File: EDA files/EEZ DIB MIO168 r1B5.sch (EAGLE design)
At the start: 302 parts, among them IC1 M24C32-WMN6P, IC10 DAC7760IPWPR, IC11 DAC7760IPWPR, IC12 OPA376AIDBVR, IC13 DAC7563TDGSR, IC14 OPA2196IDR, IC15 BTS3408G, IC16 BTS3408G, IC17 BTS3408G, IC18 BTS3408G, IC19 74HC126PW,118, IC2 Si8641BB-B-IS1, IC20 TL431B, IC21 DG468DV-T1-E3, IC22 DG468DV-T1-E3, IC23 DG468DV-T1-E3, IC24 DG468DV-T1-E3, IC25 DG468DV-T1-E3, IC26 DG468DV-T1-E3, IC27 DG468DV-T1-E3, IC28 DG468DV-T1-E3, IC29 DG468DV-T1-E3, IC3 Si8641BB-B-IS1, IC30 DG468DV-T1-E3, IC31 DG468DV-T1-E3, IC32 DG468DV-T1-E3, IC33 DG468DV-T1-E3, IC34 DG468DV-T1-E3, IC35 OPA376AIDBVR, IC36 ADS8674IDBT, IC4 L78L12, IC5 LM1117MP-5.0, IC6 LP2985-33DBVR, IC7 L79L12, IC8 STM32F446ZCT6, IC9 OPA2196IDR, J1 4907, J2 N.C., Q1 2N7002PS,115, Q10 BSS169, Q11 BSS169, Q12 BSS169, Q13 BSS169, Q2 2N7002PS,115, Q3 2N7002PS,115, Q4 2N7002PS,115, Q5 2N7002PS,115, Q6 BSS169, Q7 BSS169, Q8 BSS169, Q9 BSS169, X1 77317-104-28LF, X2 SSW-106-02-S-S, X3 691327310016, X4 691327310016, X5 1-2314878-0, X6 1-2314878-0, X7 1-2314878-0, Y1 25MHz

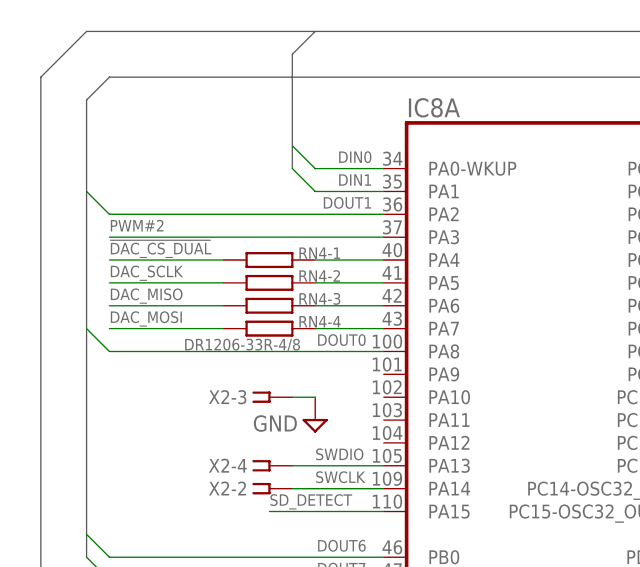
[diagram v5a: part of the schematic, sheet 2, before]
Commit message: swap DOUT0 and DOUT1
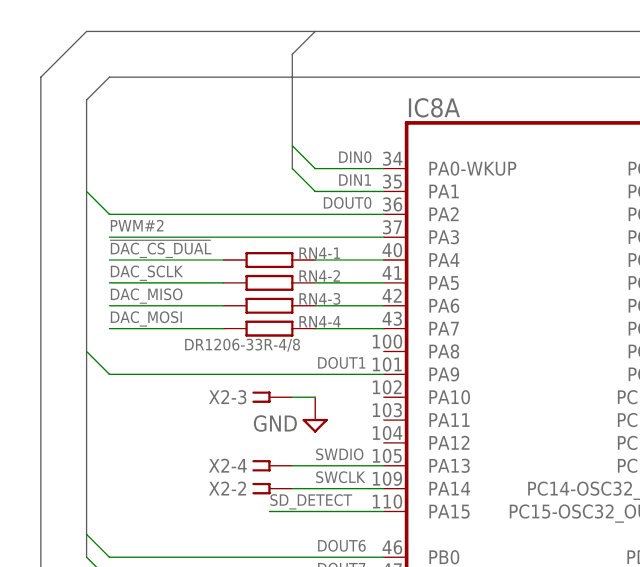
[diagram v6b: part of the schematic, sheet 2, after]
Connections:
- net DOUT0: now also IC8A.PA2; no longer IC8A.PA8
- net DOUT1: now also IC8A.PA9; no longer IC8A.PA2
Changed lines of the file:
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@@
 <setting verticaltext="up"/>
 </settings>
-<grid distance="0.025" unitdist="inch" unit="inch" style="lines" multiple="4" display="no" altdistance="0.01" altunitdist="inch" altunit="inch"/>
+<grid distance="0.1" unitdist="inch" unit="inch" style="lines" multiple="1" display="no" altdistance="0.01" altunitdist="inch" altunit="inch"/>
 <layers>
 <layer number="1" name="Top" color="4" fill="1" visible="no" active="no"/>
@@
 <net name="DOUT0" class="0">
 <segment>
-<wire x1="10.16" y1="142.24" x2="12.7" y2="139.7" width="0.1524" layer="91"/>
-<pinref part="IC8" gate="A" pin="PA8"/>
-<label x="41.275" y="140.335" size="1.27" layer="102" rot="MR0"/>
-<wire x1="12.7" y1="139.7" x2="43.18" y2="139.7" width="0.1524" layer="91"/>
-</segment>
-</net>
-<net name="DOUT1" class="0">
-<segment>
 <pinref part="IC8" gate="A" pin="PA2"/>
 <wire x1="43.18" y1="154.94" x2="12.7" y2="154.94" width="0.1524" layer="91"/>
@@
 </segment>
 </net>
+<net name="DOUT1" class="0">
+<segment>
+<wire x1="10.16" y1="139.7" x2="12.7" y2="137.16" width="0.1524" layer="91"/>
+<pinref part="IC8" gate="A" pin="PA9"/>
+<wire x1="12.7" y1="137.16" x2="43.18" y2="137.16" width="0.1524" layer="91"/>
+<label x="41.275" y="137.795" size="1.27" layer="102" rot="MR0"/>
+</segment>
+</net>
